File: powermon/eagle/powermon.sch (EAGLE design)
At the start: 41 parts, among them J1 USBSMD, J2 USBSMD, J3 TERMINAL-2, U1 LTC2943, U2 LT1764AEQ, U3 FT232RL, U4 ATMEGA328, X1 16MHz

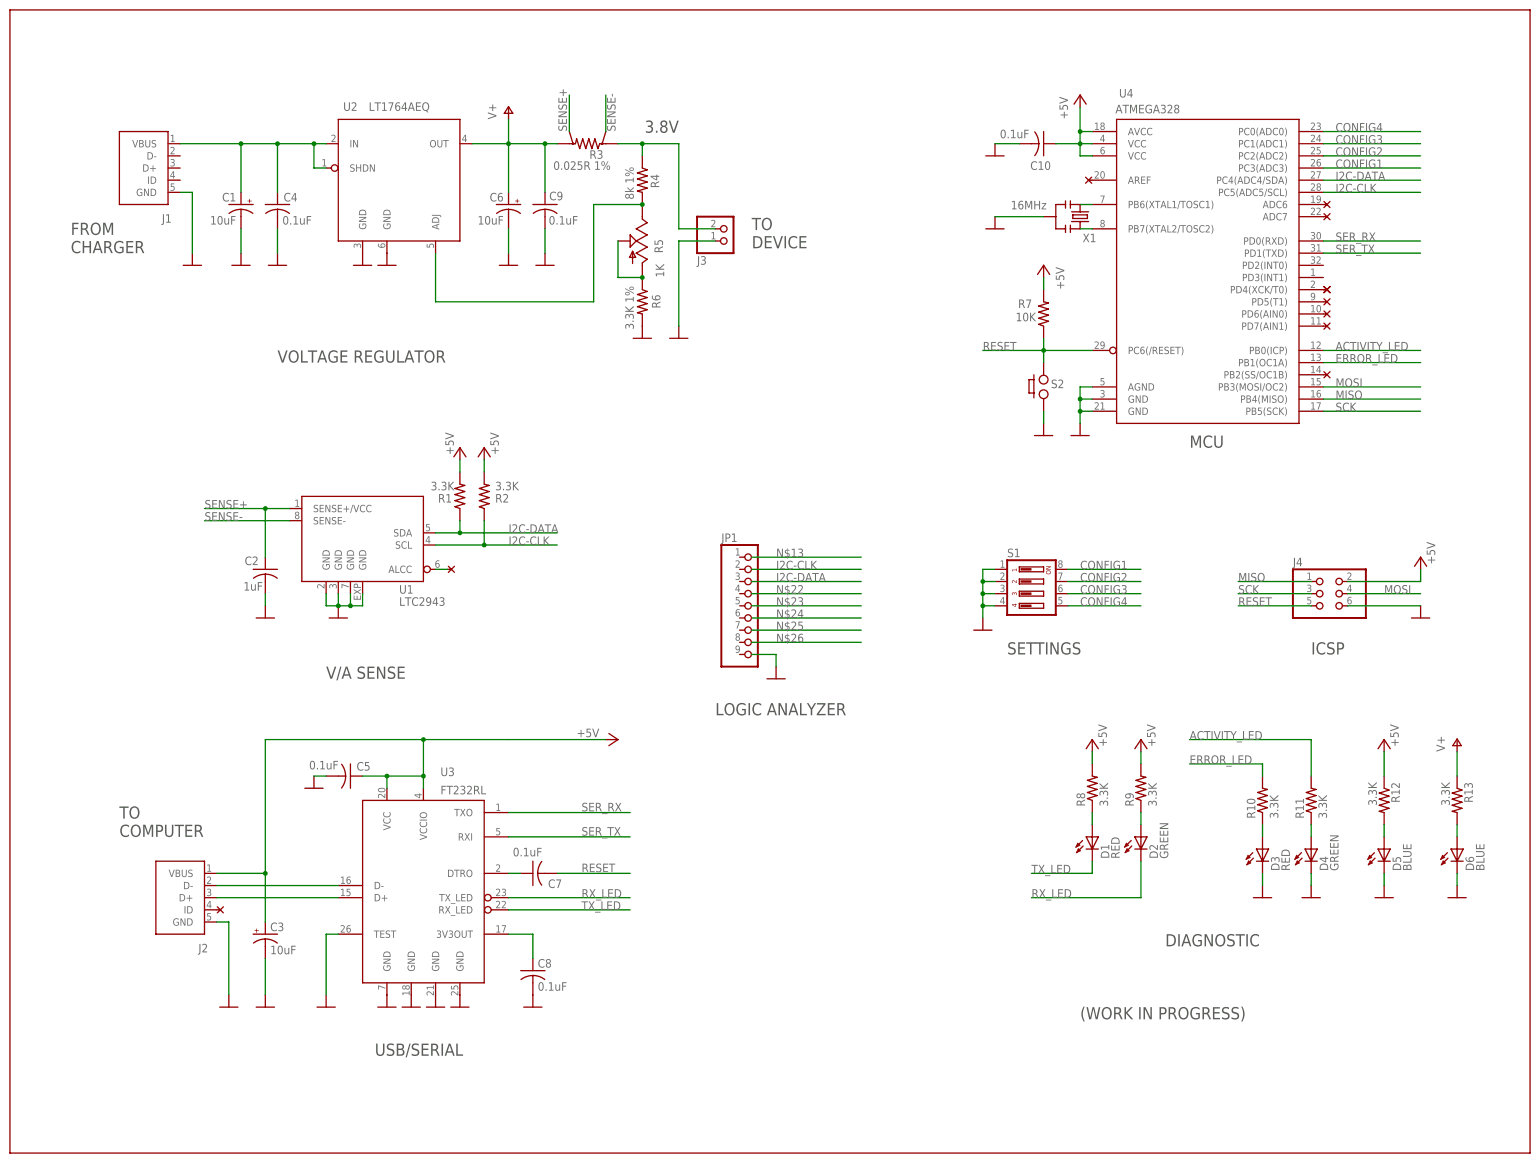
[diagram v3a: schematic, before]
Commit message: Updated the schema. This is a fully functioning one.
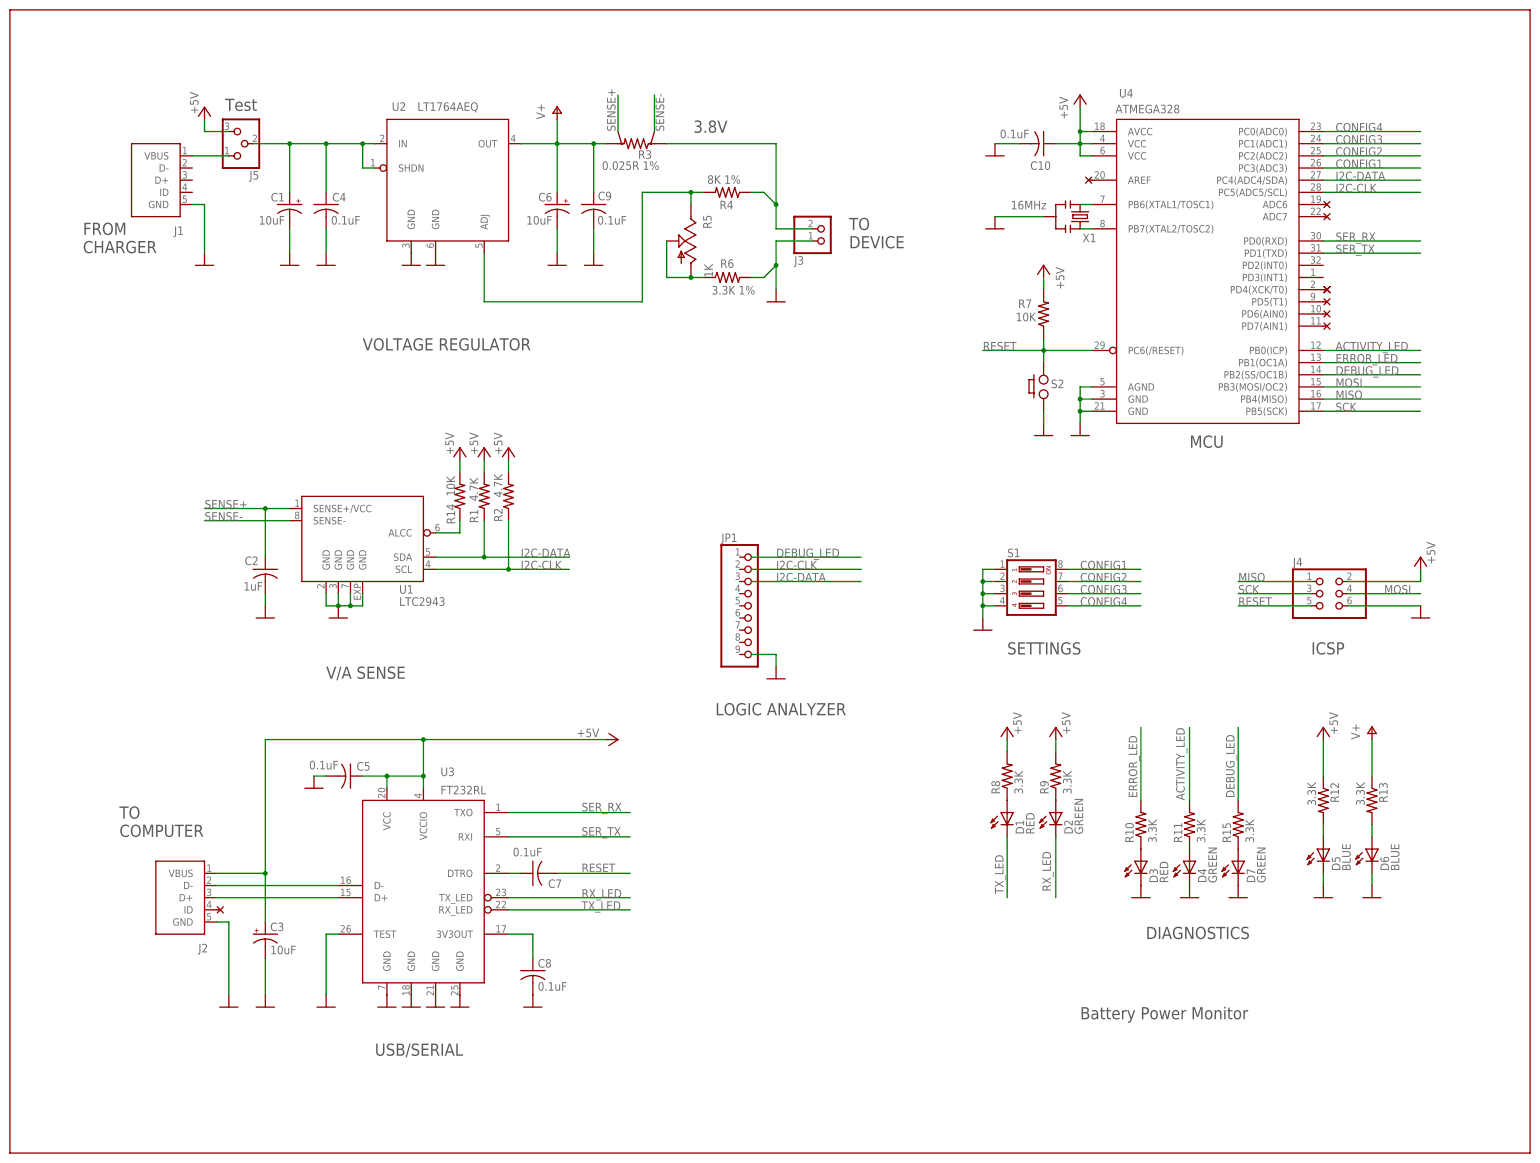
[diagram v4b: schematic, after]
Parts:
- added D7: GREEN, powermon:LED
- added J5: (no value), powermon:PINHD-1X3A
- added R14: 10K, powermon:R-US_R0805
- added R15: 3.3K, powermon:R-US_R0805
- R1, R2: value 3.3K -> 4.7K
- R4: value 8k 1% -> 8K 1%
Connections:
- new net DEBUG_LED: R15.2, U4.PB2(SS/OC1B)
- new net N$20: D7.A, R15.1
- new net N$21: J1.VBUS, J5.1
- net +5V: now also J5.3, R14.2
- net GND: now also D7.C
- net N$1: now also R14.1
- net N$9: now also J5.2; no longer J1.VBUS
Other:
- note added: "Battery Power Monitor"
- note added: "DIAGNOSTICS"
- note added: "Test"
- note removed: "(WORK IN PROGRESS)"
- note removed: "DIAGNOSTIC"
- moved on the sheet: C1, C4, C6, C9, D1, D2, D3, D4, D5, D6, J1, J3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

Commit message: Tweaked the schematic. Add a board with a rough placement.
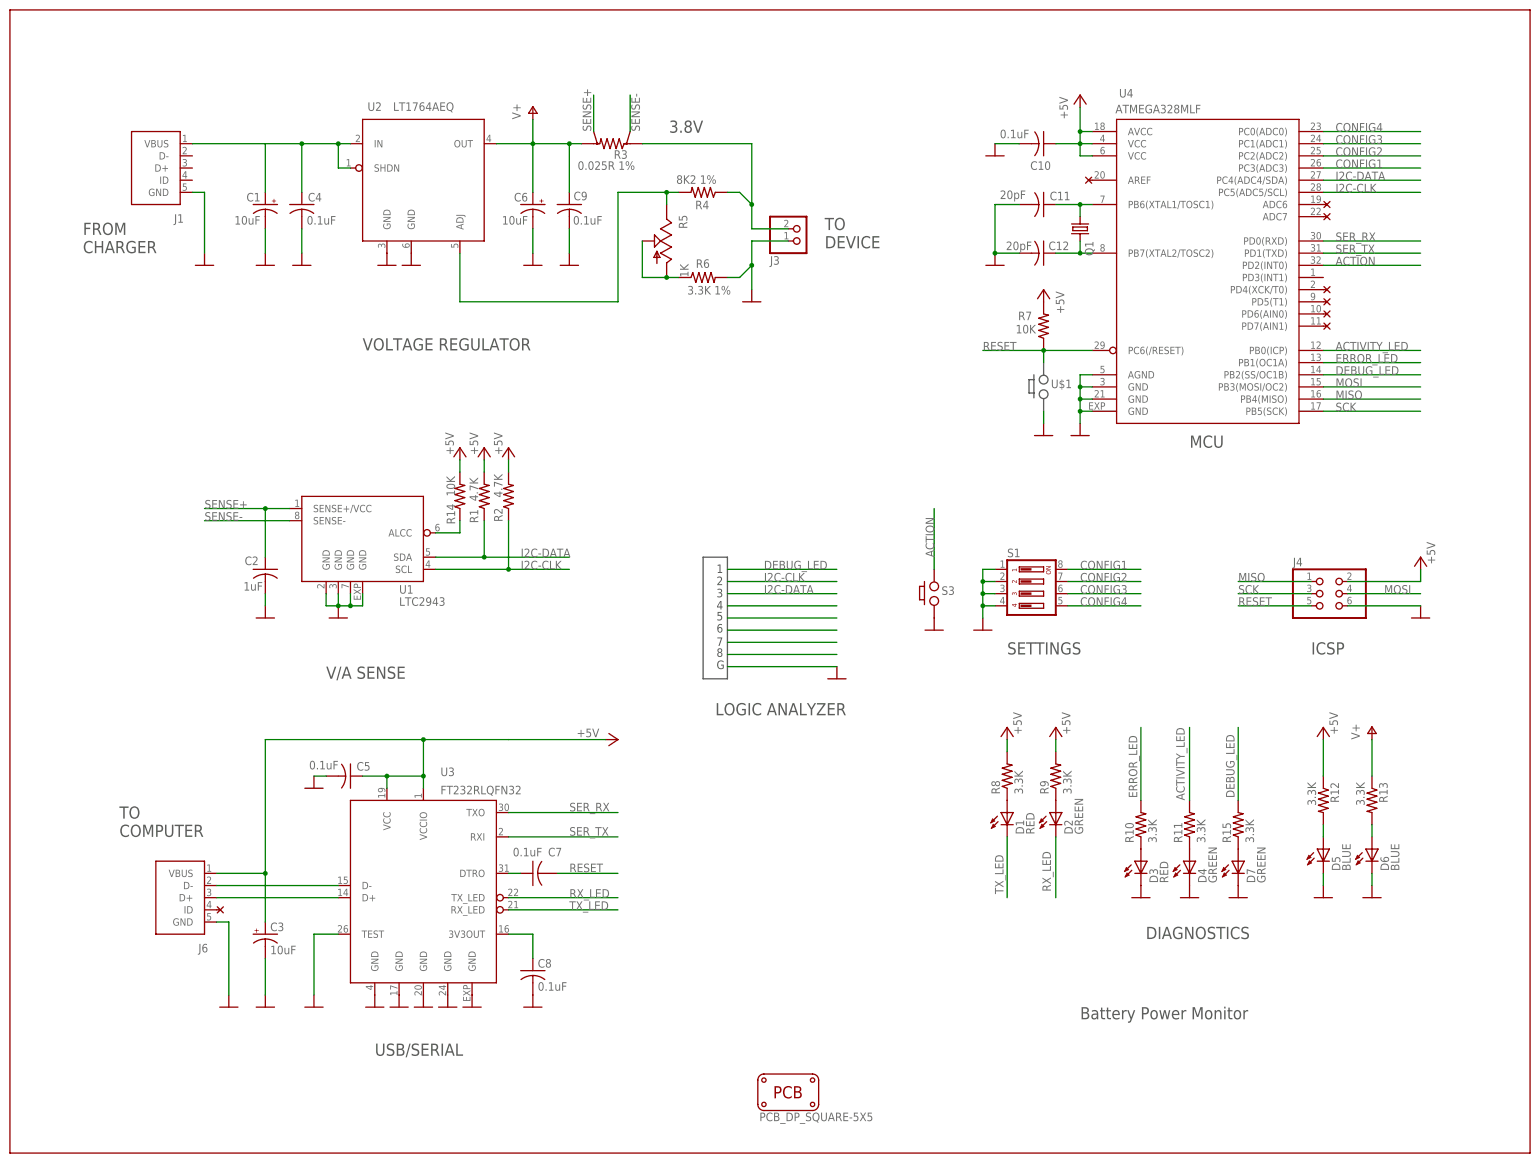
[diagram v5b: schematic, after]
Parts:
- removed J2: USBSMD, powermon:USBSMD
- removed J5: (no value), powermon:PINHD-1X3A
- removed JP1: (no value), powermon:PINHD-1X9
- removed S2: PUSH_BUTTON, powermon:PUSH_BUTTON
- removed X1: 16MHz, powermon:RESONATORSMD
- added C11, C12: 20pF, powermon:C-USC0603
- added J6: USB, powermon:USB
- added PCB1: PCB_DP_SQUARE-5X5, powermon:PCB_DP_SQUARE-5X5
- added Q1: (no value), powermon:CRYSTALCTS406
- added S3: PUSH_BUTTON, powermon:PUSH_BUTTON
- C10, C2, C4, C5, C7, C9: device powermon:C-USC0805 -> powermon:C-USC0603
- C8: device analyzer:C-USC0805 -> powermon:C-USC0603
- J1: value USBSMD -> USB; device powermon:USBSMD -> powermon:USB
- R1, R10, R11, R12, R13, R14, R15, R2, R6, R7, R8, R9: device powermon:R-US_R0805 -> powermon:R-US_R0603
- R4: value 8K 1% -> 8K2 1%; device powermon:R-US_R0805 -> powermon:R-US_R0603
- U3: value FT232RL -> FT232RLQFN32; device powermon:FT232RL -> powermon:FT232RLQFN32
- U4: value ATMEGA328 -> ATMEGA328MLF; device powermon:ATMEGA328 -> powermon:ATMEGA328MLF
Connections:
- new net ACTION: S3.P$3, U4.PD2(INT0)
- net +5V: no longer J5.3
- net GND: now also C11.2, C12.2, J6.GND, S3.P$4, U3.GND@5, U4.GND@3; no longer J2.GND, S2.P$4, X1.2
- net N$10: now also J6.D+; no longer J2.D+
- net N$12: now also J6.VBUS; no longer J2.VBUS
- net N$15: now also J6.D-; no longer J2.D-
- net N$2: now also C11.1, Q1.1, U4.PB6(XTAL1/TOSC1); no longer U4.PB7(XTAL2/TOSC2), X1.1
- net N$21: no longer J5.1
- net N$7: now also C12.1, Q1.2, U4.PB7(XTAL2/TOSC2); no longer U4.PB6(XTAL1/TOSC1), X1.3
- net N$9: no longer J5.2
- net RESET: no longer S2.P$3
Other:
- note added: "1"
- note added: "2"
- note added: "3"
- note added: "4"
- note added: "5"
- note added: "6"
- note added: "7"
- note added: "8"
- note added: "G"
- note removed: "Test"
- moved on the sheet: C1, C4, C6, C9, J1, J3, R3, R4, R5, R6, R7, U2

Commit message: Done initial routing of manual nets. Incomplete.
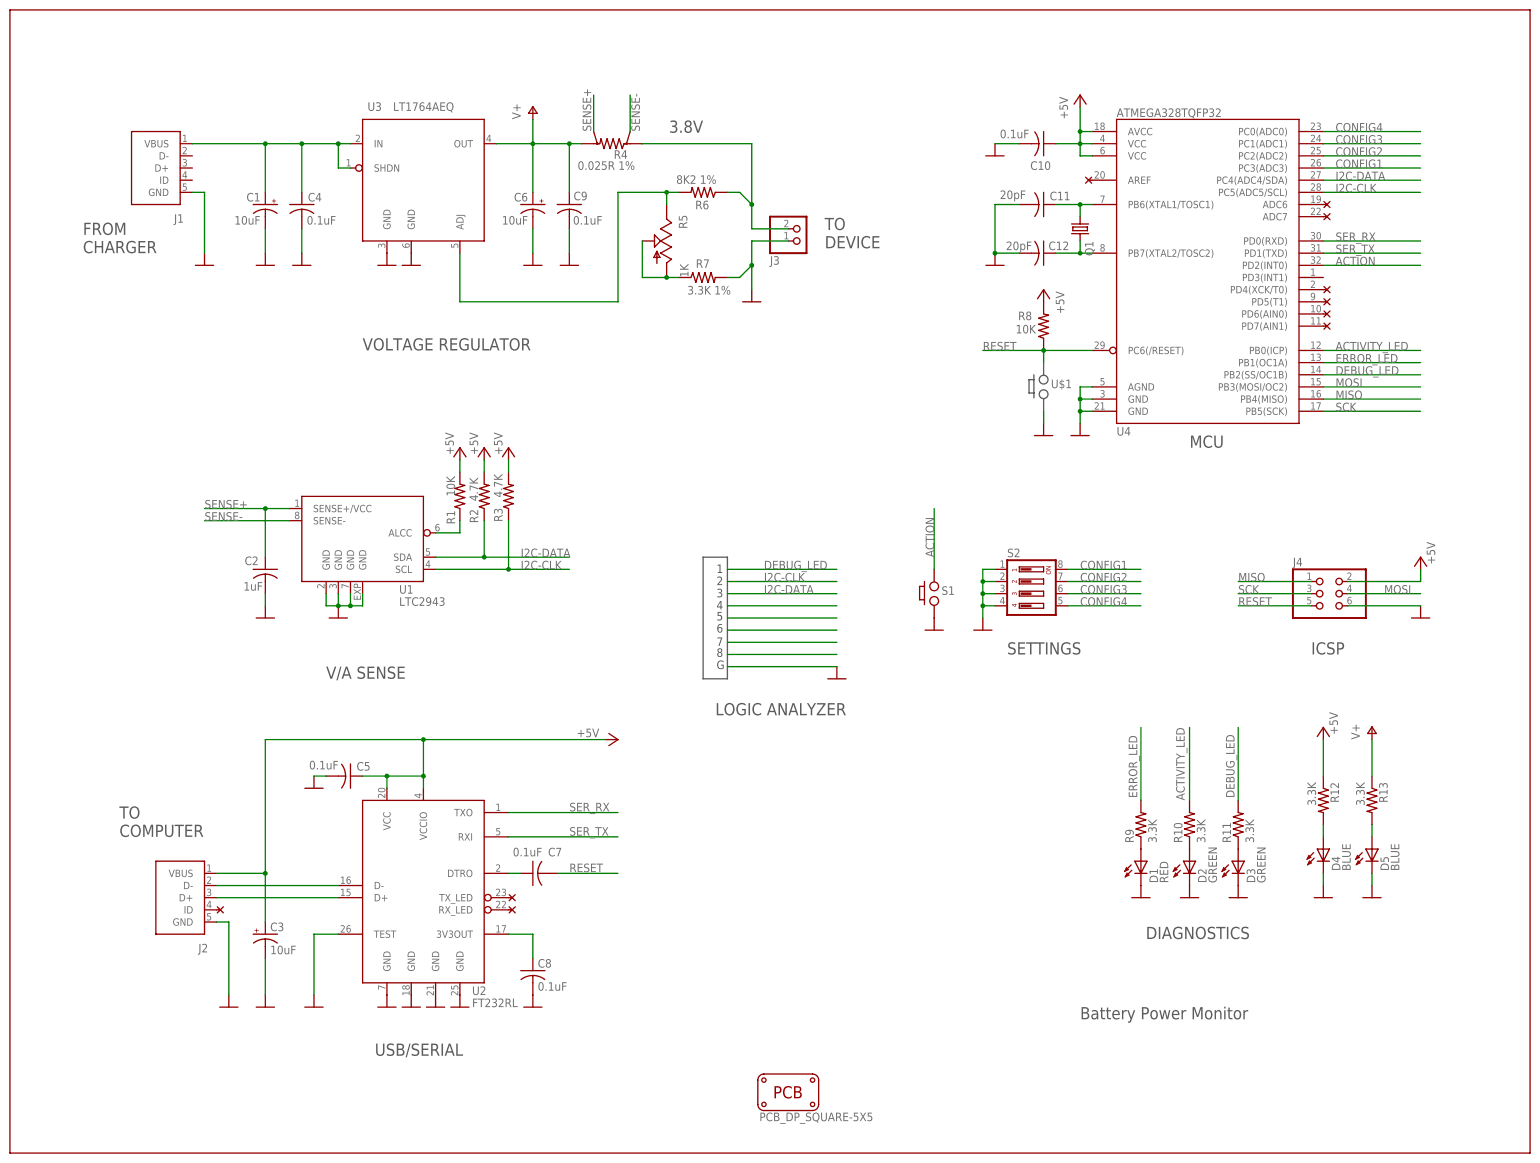
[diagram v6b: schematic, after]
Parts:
- removed D6: BLUE, powermon:LED
- removed D7: GREEN, powermon:LED
- removed R14: 10K, powermon:R-US_R0603
- removed R15: 3.3K, powermon:R-US_R0603
- removed S3: PUSH_BUTTON, powermon:PUSH_BUTTON
- added S2: 219-04, powermon:219-04
- D3: value RED -> GREEN
- D4: value GREEN -> BLUE
- R1: value 4.7K -> 10K
- R3: value 0.025R 1% -> 4.7K; device powermon:SHUNT -> powermon:R-US_R0603
- R4: value 8K2 1% -> 0.025R 1%; device powermon:R-US_R0603 -> powermon:SHUNT
- R6: value 3.3K 1% -> 8K2 1%
- R7: value 10K -> 3.3K 1%
- R8: value 3.3K -> 10K
- S1: value 219-04 -> PUSH_BUTTON; device powermon:219-04 -> powermon:PUSH_BUTTON
- U2: value LT1764AEQ -> FT232RL; device powermon:LTE1764 -> powermon:FT232RL
- U3: value FT232RLQFN32 -> LT1764AEQ; device powermon:FT232RLQFN32 -> powermon:LTE1764
- U4: value ATMEGA328MLF -> ATMEGA328TQFP32; device powermon:ATMEGA328MLF -> powermon:ATMEGA328TQFP32
- renumbered J6 to J2
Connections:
- removed net GND@3: U1.GND@2, U1.GND@3, U1.GND@7, U1.GND@9
- removed net N$12: C3.+, C5.1, J2.VBUS, U3.VCC, U3.VCCIO
- removed net N$21: J1.VBUS
- removed net N$6: D1.A, R8.1
- removed net N$8: D2.A, R9.1
- removed net RX_LED: D2.C, U3.TX_LED
- removed net TX_LED: D1.C, U3.RX_LED
- net +5V: now also C3.+, C5.1, J2.VBUS, R3.2, U2.VCC, U2.VCCIO; no longer R14.2, R7.2, R9.2
- net ACTION: now also S1.P$3; no longer S3.P$3
- net ACTIVITY_LED: now also R10.2; no longer R11.2
- net CONFIG1: now also S2.8; no longer S1.8
- net CONFIG2: now also S2.7; no longer S1.7
- net CONFIG3: now also S2.6; no longer S1.6
- net CONFIG4: now also S2.5; no longer S1.5
- net DEBUG_LED: now also R11.2; no longer R15.2
- net ERROR_LED: now also R9.2; no longer R10.2
- net GND: now also D1.C, D2.C, R7.2, S1.P$4, S2.1, S2.2, S2.3, S2.4, U1.GND@2, U1.GND@3, U1.GND@7, U1.GND@9, U2.GND@3, U2.GND@4, U2.TEST; no longer D6.C, D7.C, R6.2, S1.1, S1.2, S1.3, S1.4, S3.P$4, U3.GND@3, U3.GND@4, U3.GND@5, U3.TEST, U4.GND@3
- net I2C-CLK: now also R3.1; no longer R2.1
- net I2C-DATA: now also R2.1; no longer R1.1
- net N$1: now also R1.1; no longer R14.1
- net N$10: now also U2.D+; no longer U3.D+
- net N$11: now also U2.DTRO; no longer U3.DTRO
- net N$14: now also D5.A; no longer D6.A
- net N$15: now also U2.D-; no longer U3.D-
- net N$16: now also U2.3V3OUT; no longer U3.3V3OUT
- net N$17: now also D4.A; no longer D5.A
- net N$18: now also R7.1; no longer R6.1
- net N$19: now also R6.2, U3.ADJ; no longer R4.2, U2.ADJ
- net N$20: now also D3.A, R11.1; no longer D7.A, R15.1
- net N$22: now also R4.I1, R6.1; no longer R3.I1, R4.1
- net N$3: now also D2.A, R10.1; no longer D4.A, R11.1
- net N$4: now also D1.A, R9.1; no longer D3.A, R10.1
- net N$9: now also J1.VBUS, U3.IN, U3.SHDN; no longer U2.IN, U2.SHDN
- net RESET: now also R8.1; no longer R7.1
- net SENSE+: now also R4.V2; no longer R3.V2
- net SENSE-: now also R4.V1; no longer R3.V1
- net SER_RX: now also U2.TXO; no longer U3.TXO
- net SER_TX: now also U2.RXI; no longer U3.RXI
- net V+: now also R4.I2, U3.OUT; no longer R3.I2, U2.OUT
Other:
- moved on the sheet: D1, D2, D3, D4, D5, R1, R10, R11, R2, R6, R7, R8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

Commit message: Added footprints, tweaked the placement. Work in progress.
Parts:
- S1: value PUSH_BUTTON -> PUSH_BUTTONEVQPSL; device powermon:PUSH_BUTTON -> powermon:PUSH_BUTTONEVQPSL
- U1: device powermon:LTC2943SMD -> powermon:LTC2943
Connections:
- net ACTION: now also S1.2; no longer S1.P$3
- net GND: now also S1.1; no longer S1.P$4
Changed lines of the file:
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@@
 <part name="J3" library="powermon" deviceset="TERMINAL-2" device=""/>
 <part name="R5" library="powermon" deviceset="TRIM_US-" device="SM-42/43A" value="1K"/>
-<part name="U1" library="powermon" deviceset="LTC2943" device="" technology="SMD" value="LTC2943"/>
+<part name="U1" library="powermon" deviceset="LTC2943" device="" value="LTC2943"/>
 <part name="GND17" library="powermon" deviceset="GND" device=""/>
 <part name="D5" library="powermon" deviceset="LED" device="" value="BLUE"/>
@@
 <part name="GND32" library="powermon" deviceset="GND" device=""/>
 <part name="R11" library="powermon" deviceset="R-US_" device="R0603" value="3.3K"/>
-<part name="S1" library="powermon" deviceset="PUSH_BUTTON" device=""/>
+<part name="S1" library="powermon" deviceset="PUSH_BUTTON" device="EVQPSL"/>
 <part name="GND22" library="powermon" deviceset="GND" device=""/>
 <part name="J2" library="powermon" deviceset="USB" device=""/>
@@
 </segment>
 <segment>
-<pinref part="S1" gate="G$1" pin="P$4"/>
+<pinref part="S1" gate="G$1" pin="1"/>
 <pinref part="GND22" gate="1" pin="GND"/>
 </segment>
@@
 </segment>
 <segment>
-<pinref part="S1" gate="G$1" pin="P$3"/>
+<pinref part="S1" gate="G$1" pin="2"/>
 <wire x1="157.48" y1="121.92" x2="157.48" y2="134.62" width="0.1524" layer="91"/>
 <label x="157.48" y="124.46" size="1.778" layer="95" rot="R90"/>
